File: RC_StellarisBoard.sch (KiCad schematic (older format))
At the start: 17 parts, among them K1 CONN_3, K2 CONN_3, K3 CONN_3, K4 CONN_3, P1 CONN_2

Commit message: brd + sch
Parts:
- gave numbers to parts that had none: 4
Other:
- moved on the sheet: P1
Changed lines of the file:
@@
 L CONN_2 P1
 U 1 1 52C8995E
-P 3800 2550
-F 0 "P1" V 3750 2550 40  0000 C CNN
-F 1 "CONN_2" V 3850 2550 40  0000 C CNN
-F 2 "" H 3800 2550 60  0000 C CNN
-F 3 "" H 3800 2550 60  0000 C CNN
-	1    3800 2550
+P 4550 1000
+F 0 "P1" V 4500 1000 40  0000 C CNN
+F 1 "CONN_2" V 4600 1000 40  0000 C CNN
+F 2 "" H 4550 1000 60  0000 C CNN
+F 3 "" H 4550 1000 60  0000 C CNN
+	1    4550 1000
 	1    0    0    -1
 $EndComp
@@
 L +3.3V #PWR01
 U 1 1 52C899F7
-P 3450 2450
-F 0 "#PWR01" H 3450 2410 30  0001 C CNN
-F 1 "+3.3V" H 3450 2560 30  0000 C CNN
-F 2 "" H 3450 2450 60  0000 C CNN
-F 3 "" H 3450 2450 60  0000 C CNN
-	1    3450 2450
+P 4200 900
+F 0 "#PWR01" H 4200 860 30  0001 C CNN
+F 1 "+3.3V" H 4200 1010 30  0000 C CNN
+F 2 "" H 4200 900 60  0000 C CNN
+F 3 "" H 4200 900 60  0000 C CNN
+	1    4200 900
 	1    0    0    -1
 $EndComp
@@
 L +5V #PWR02
 U 1 1 52C89A0A
-P 3450 2650
-F 0 "#PWR02" H 3450 2740 20  0001 C CNN
-F 1 "+5V" H 3450 2740 30  0000 C CNN
-F 2 "" H 3450 2650 60  0000 C CNN
-F 3 "" H 3450 2650 60  0000 C CNN
-	1    3450 2650
+P 4200 1100
+F 0 "#PWR02" H 4200 1190 20  0001 C CNN
+F 1 "+5V" H 4200 1190 30  0000 C CNN
+F 2 "" H 4200 1100 60  0000 C CNN
+F 3 "" H 4200 1100 60  0000 C CNN
+	1    4200 1100
 	1    0    0    -1
 $EndComp
@@
 PWM1
 $Comp
-L CONN_1 P?
+L CONN_1 P2
 U 1 1 52C89C4A
 P 800 1700
-F 0 "P?" H 880 1700 40  0000 L CNN
+F 0 "P2" H 880 1700 40  0000 L CNN
 F 1 "CONN_1" H 800 1755 30  0001 C CNN
 F 2 "" H 800 1700 60  0000 C CNN
@@
 $EndComp
 $Comp
-L CONN_1 P?
+L CONN_1 P3
 U 1 1 52C89C57
 P 800 1800
-F 0 "P?" H 880 1800 40  0000 L CNN
+F 0 "P3" H 880 1800 40  0000 L CNN
 F 1 "CONN_1" H 800 1855 30  0001 C CNN
 F 2 "" H 800 1800 60  0000 C CNN
@@
 $EndComp
 $Comp
-L CONN_1 P?
+L CONN_1 P4
 U 1 1 52C89C5D
 P 800 1900
-F 0 "P?" H 880 1900 40  0000 L CNN
+F 0 "P4" H 880 1900 40  0000 L CNN
 F 1 "CONN_1" H 800 1955 30  0001 C CNN
 F 2 "" H 800 1900 60  0000 C CNN
@@
 $EndComp
 $Comp
-L CONN_1 P?
+L CONN_1 P5
 U 1 1 52C89C63
 P 800 2000
-F 0 "P?" H 880 2000 40  0000 L CNN
+F 0 "P5" H 880 2000 40  0000 L CNN
 F 1 "CONN_1" H 800 2055 30  0001 C CNN
 F 2 "" H 800 2000 60  0000 C CNN

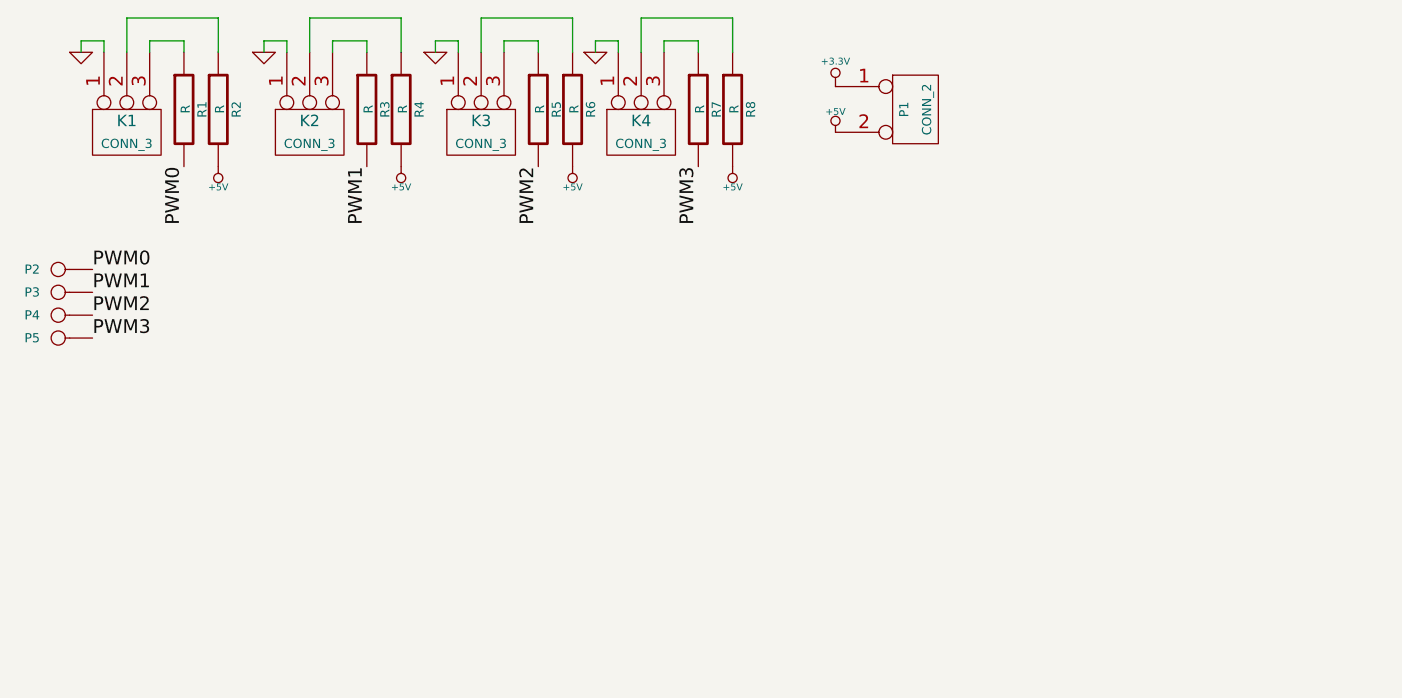
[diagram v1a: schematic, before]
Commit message: brd + sch (amc6821 + mosfet)
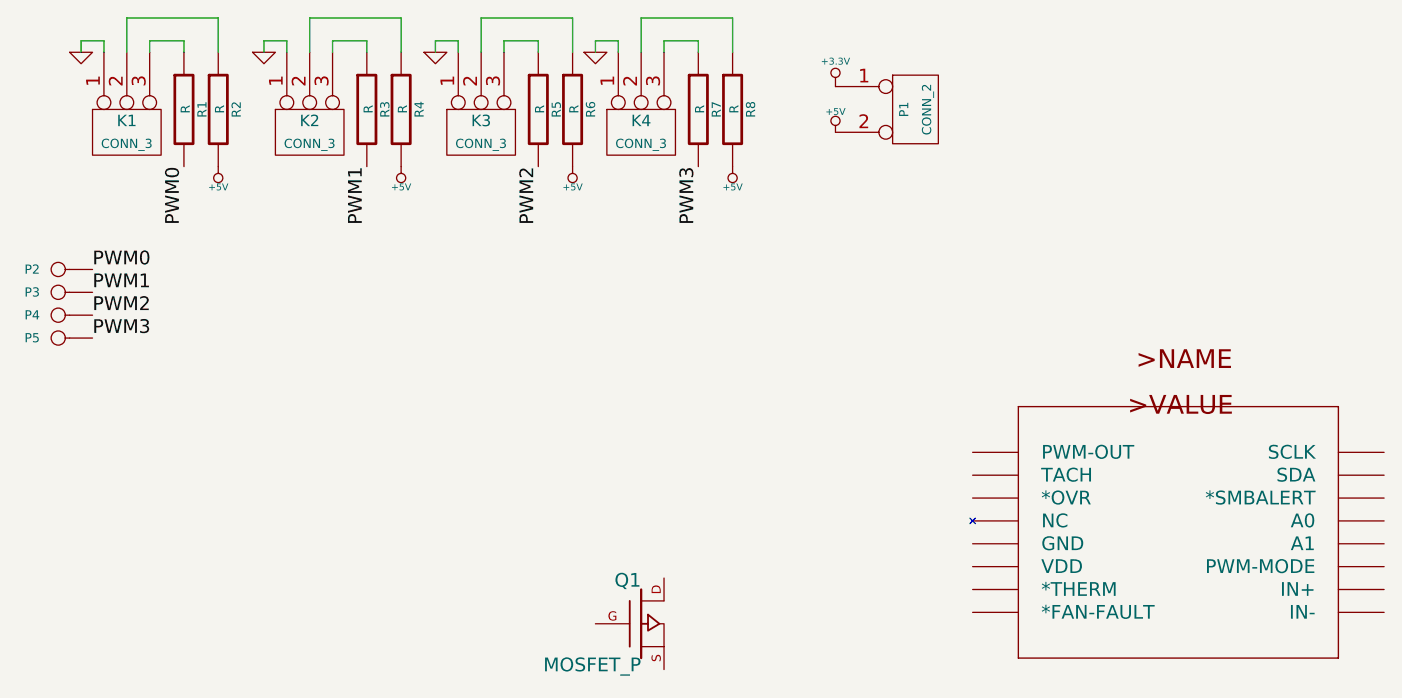
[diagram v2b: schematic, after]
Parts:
- added Q1: MOSFET_P, ~, symbol MOSFET_P
- added U1: AMC6821_DBQ_16_DBQ16, symbol AMC6821_DBQ_16_DBQ16
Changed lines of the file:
@@
 LIBS:contrib
 LIBS:valves
+LIBS:amc6821
+LIBS:RC_StellarisBoard-cache
 EELAYER 27 0
 EELAYER END
@@
 Sheet 1 1
 Title ""
-Date "4 jan 2014"
+Date "5 jan 2014"
 Rev ""
 Comp ""
@@
 $EndComp
 $Comp
-L +3.3V #PWR01
+L +3.3V #PWR9
 U 1 1 52C899F7
 P 4200 900
-F 0 "#PWR01" H 4200 860 30  0001 C CNN
+F 0 "#PWR9" H 4200 860 30  0001 C CNN
 F 1 "+3.3V" H 4200 1010 30  0000 C CNN
 F 2 "" H 4200 900 60  0000 C CNN
@@
 $EndComp
 $Comp
-L +5V #PWR02
+L +5V #PWR10
 U 1 1 52C89A0A
 P 4200 1100
-F 0 "#PWR02" H 4200 1190 20  0001 C CNN
+F 0 "#PWR10" H 4200 1190 20  0001 C CNN
 F 1 "+5V" H 4200 1190 30  0000 C CNN
 F 2 "" H 4200 1100 60  0000 C CNN
@@
 $EndComp
 $Comp
-L GND #PWR03
+L GND #PWR1
 U 1 1 52C89A60
 P 900 750
-F 0 "#PWR03" H 900 750 30  0001 C CNN
+F 0 "#PWR1" H 900 750 30  0001 C CNN
 F 1 "GND" H 900 680 30  0001 C CNN
 F 2 "" H 900 750 60  0000 C CNN
@@
 	1000 700  1000 750
 $Comp
-L GND #PWR04
+L GND #PWR3
 U 1 1 52C89A70
 P 1700 750
-F 0 "#PWR04" H 1700 750 30  0001 C CNN
+F 0 "#PWR3" H 1700 750 30  0001 C CNN
 F 1 "GND" H 1700 680 30  0001 C CNN
 F 2 "" H 1700 750 60  0000 C CNN
@@
 $EndComp
 $Comp
-L GND #PWR05
+L GND #PWR5
 U 1 1 52C89A76
 P 2450 750
-F 0 "#PWR05" H 2450 750 30  0001 C CNN
+F 0 "#PWR5" H 2450 750 30  0001 C CNN
 F 1 "GND" H 2450 680 30  0001 C CNN
 F 2 "" H 2450 750 60  0000 C CNN
@@
 $EndComp
 $Comp
-L GND #PWR06
+L GND #PWR7
 U 1 1 52C89A7C
 P 3150 750
-F 0 "#PWR06" H 3150 750 30  0001 C CNN
+F 0 "#PWR7" H 3150 750 30  0001 C CNN
 F 1 "GND" H 3150 680 30  0001 C CNN
 F 2 "" H 3150 750 60  0000 C CNN
@@
 	3450 700  3450 750
 $Comp
-L +5V #PWR07
+L +5V #PWR2
 U 1 1 52C89B9E
 P 1500 1250
-F 0 "#PWR07" H 1500 1340 20  0001 C CNN
+F 0 "#PWR2" H 1500 1340 20  0001 C CNN
 F 1 "+5V" H 1500 1340 30  0000 C CNN
 F 2 "" H 1500 1250 60  0000 C CNN
@@
 $EndComp
 $Comp
-L +5V #PWR08
+L +5V #PWR4
 U 1 1 52C89BA4
 P 2300 1250
-F 0 "#PWR08" H 2300 1340 20  0001 C CNN
+F 0 "#PWR4" H 2300 1340 20  0001 C CNN
 F 1 "+5V" H 2300 1340 30  0000 C CNN
 F 2 "" H 2300 1250 60  0000 C CNN
@@
 $EndComp
 $Comp
-L +5V #PWR09
+L +5V #PWR6
 U 1 1 52C89BAA
 P 3050 1250
-F 0 "#PWR09" H 3050 1340 20  0001 C CNN
+F 0 "#PWR6" H 3050 1340 20  0001 C CNN
 F 1 "+5V" H 3050 1340 30  0000 C CNN
 F 2 "" H 3050 1250 60  0000 C CNN
@@
 $EndComp
 $Comp
-L +5V #PWR010
+L +5V #PWR8
 U 1 1 52C89BB0
 P 3750 1250
-F 0 "#PWR010" H 3750 1340 20  0001 C CNN
+F 0 "#PWR8" H 3750 1340 20  0001 C CNN
 F 1 "+5V" H 3750 1340 30  0000 C CNN
 F 2 "" H 3750 1250 60  0000 C CNN
@@
 Text Label 950  2000 0    60   ~ 0
 PWM3
+$Comp
+L AMC6821_DBQ_16_DBQ16 U1
+U 1 1 52C8A2FB
+P 5700 2800
+F 0 "U1" H 5700 2800 60  0001 C CNN
+F 1 "AMC6821_DBQ_16_DBQ16" H 5700 2800 60  0001 C CNN
+F 2 "" H 5700 2800 60  0000 C CNN
+F 3 "" H 5700 2800 60  0000 C CNN
+	1    5700 2800
+	1    0    0    -1
+$EndComp
+$Comp
+L MOSFET_P Q1
+U 1 1 52C8A420
+P 3350 3250
+F 0 "Q1" H 3350 3440 60  0000 R CNN
+F 1 "MOSFET_P" H 3350 3070 60  0000 R CNN
+F 2 "~" H 3350 3250 60  0000 C CNN
+F 3 "~" H 3350 3250 60  0000 C CNN
+	1    3350 3250
+	1    0    0    -1
+$EndComp
 $EndSCHEMATC
